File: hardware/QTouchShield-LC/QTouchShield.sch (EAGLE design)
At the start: 59 parts, among them IC1 AT32UC3C0512CJEDEC-MS-026, J1 SNS00...07, J10 CAPS08...15, J11 CAPS24...31, J12 CAPS16...23, J13 SPI-MEGA, J14 SPI-UNO, J15 COMMS Select, J16 DETECT00...15, J17 DETECT16...31, J18 JTAG, J19 TOUCH DATA, J2 SNS08...15, J3 SNS16...23, J4 SNS24...31, J5 RES00...07, J6 RES08...15, J7 RES16...23, J8 RES24...31, J9 CAPS00...07, Q1 BSS138, Q2 BSS138, Q3 BSS138, Q4 BSS138, Q5 BSS138, Q6 BSS138, U1 ARDUINO-2560-MEGA-R3-SMD, X1 Firmware Upgrade Port

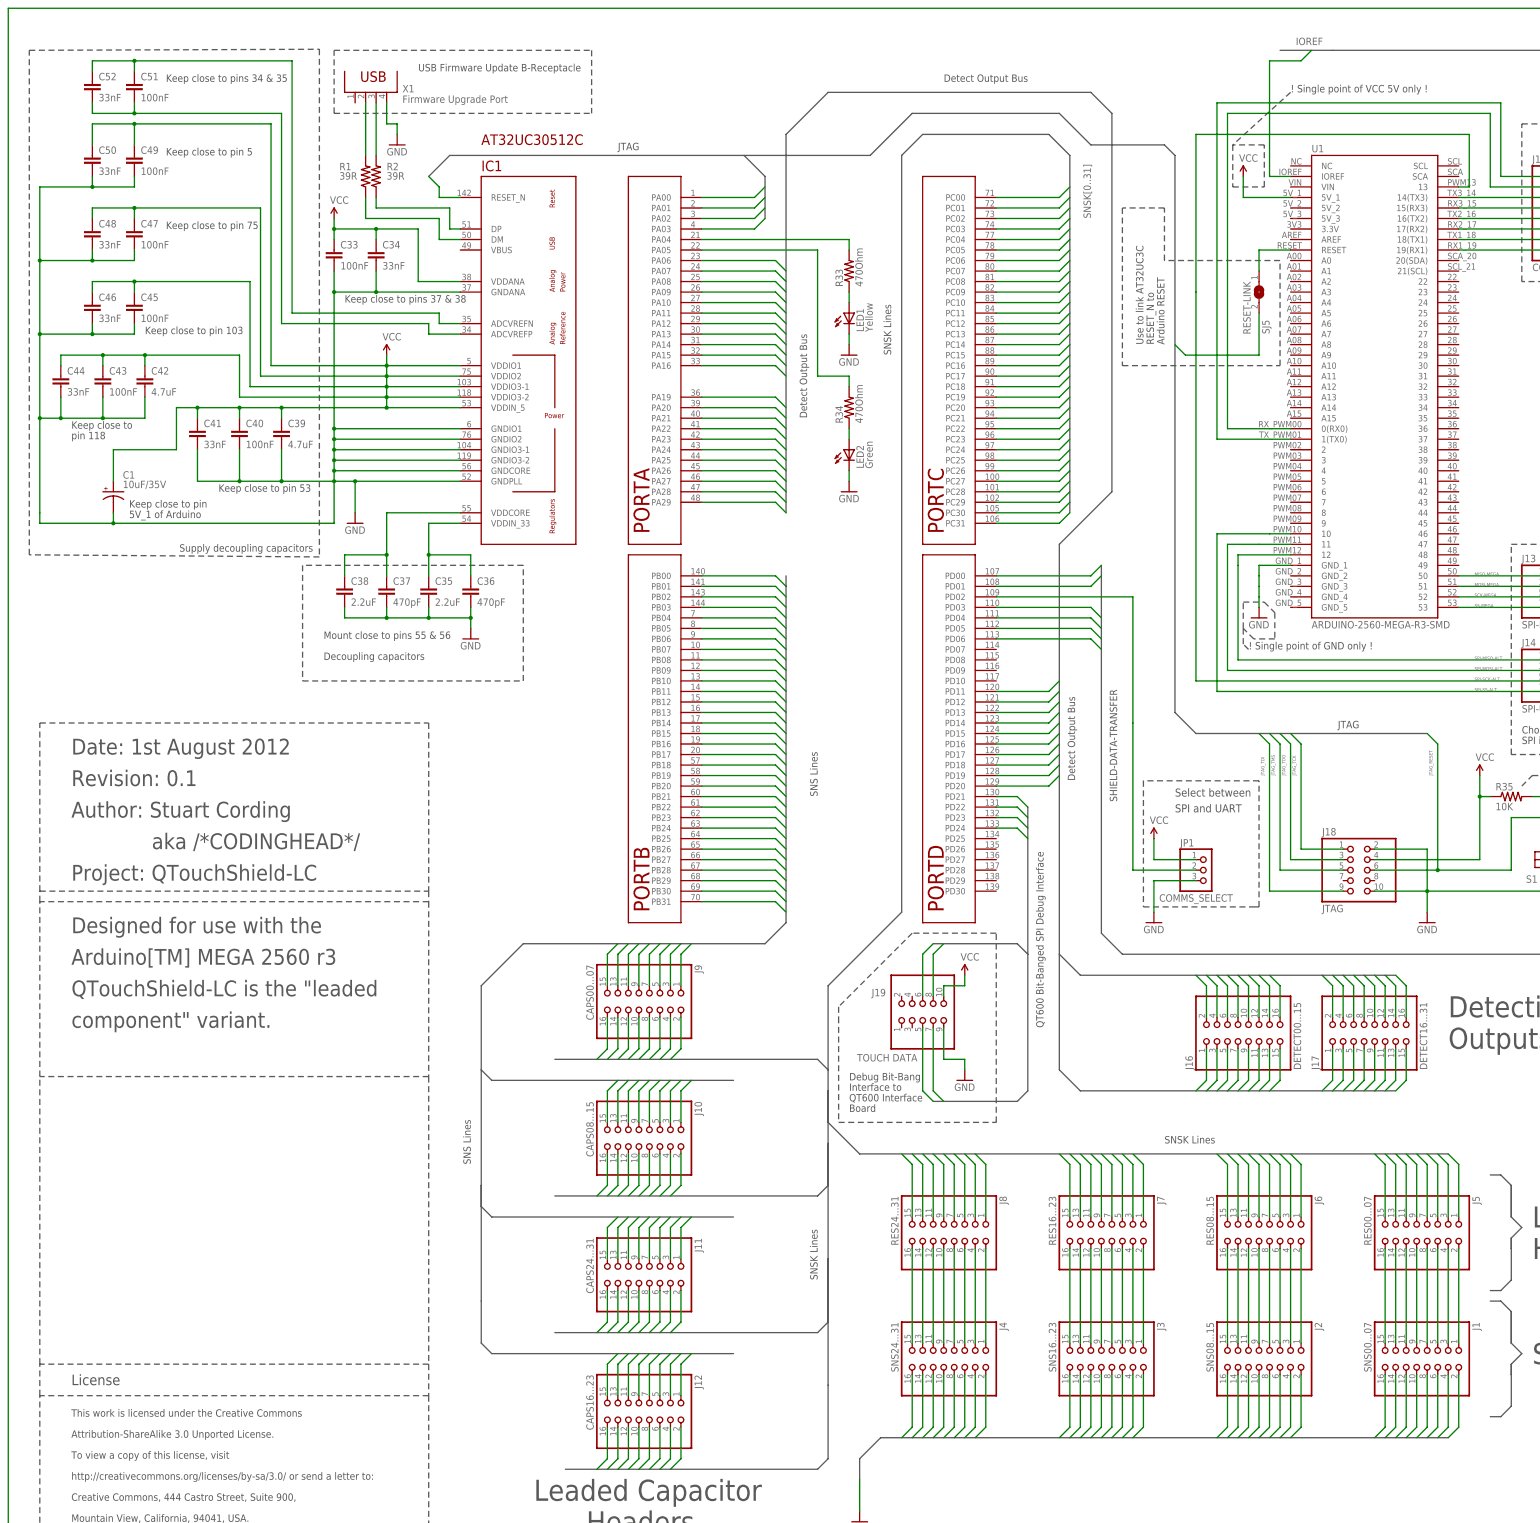
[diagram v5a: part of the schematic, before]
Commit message: Final routed board for LC version.
Board finally routed with the LC layout.
No known major issues to resolve.
Consider only ground-plane under MCU and review from STROHAL.
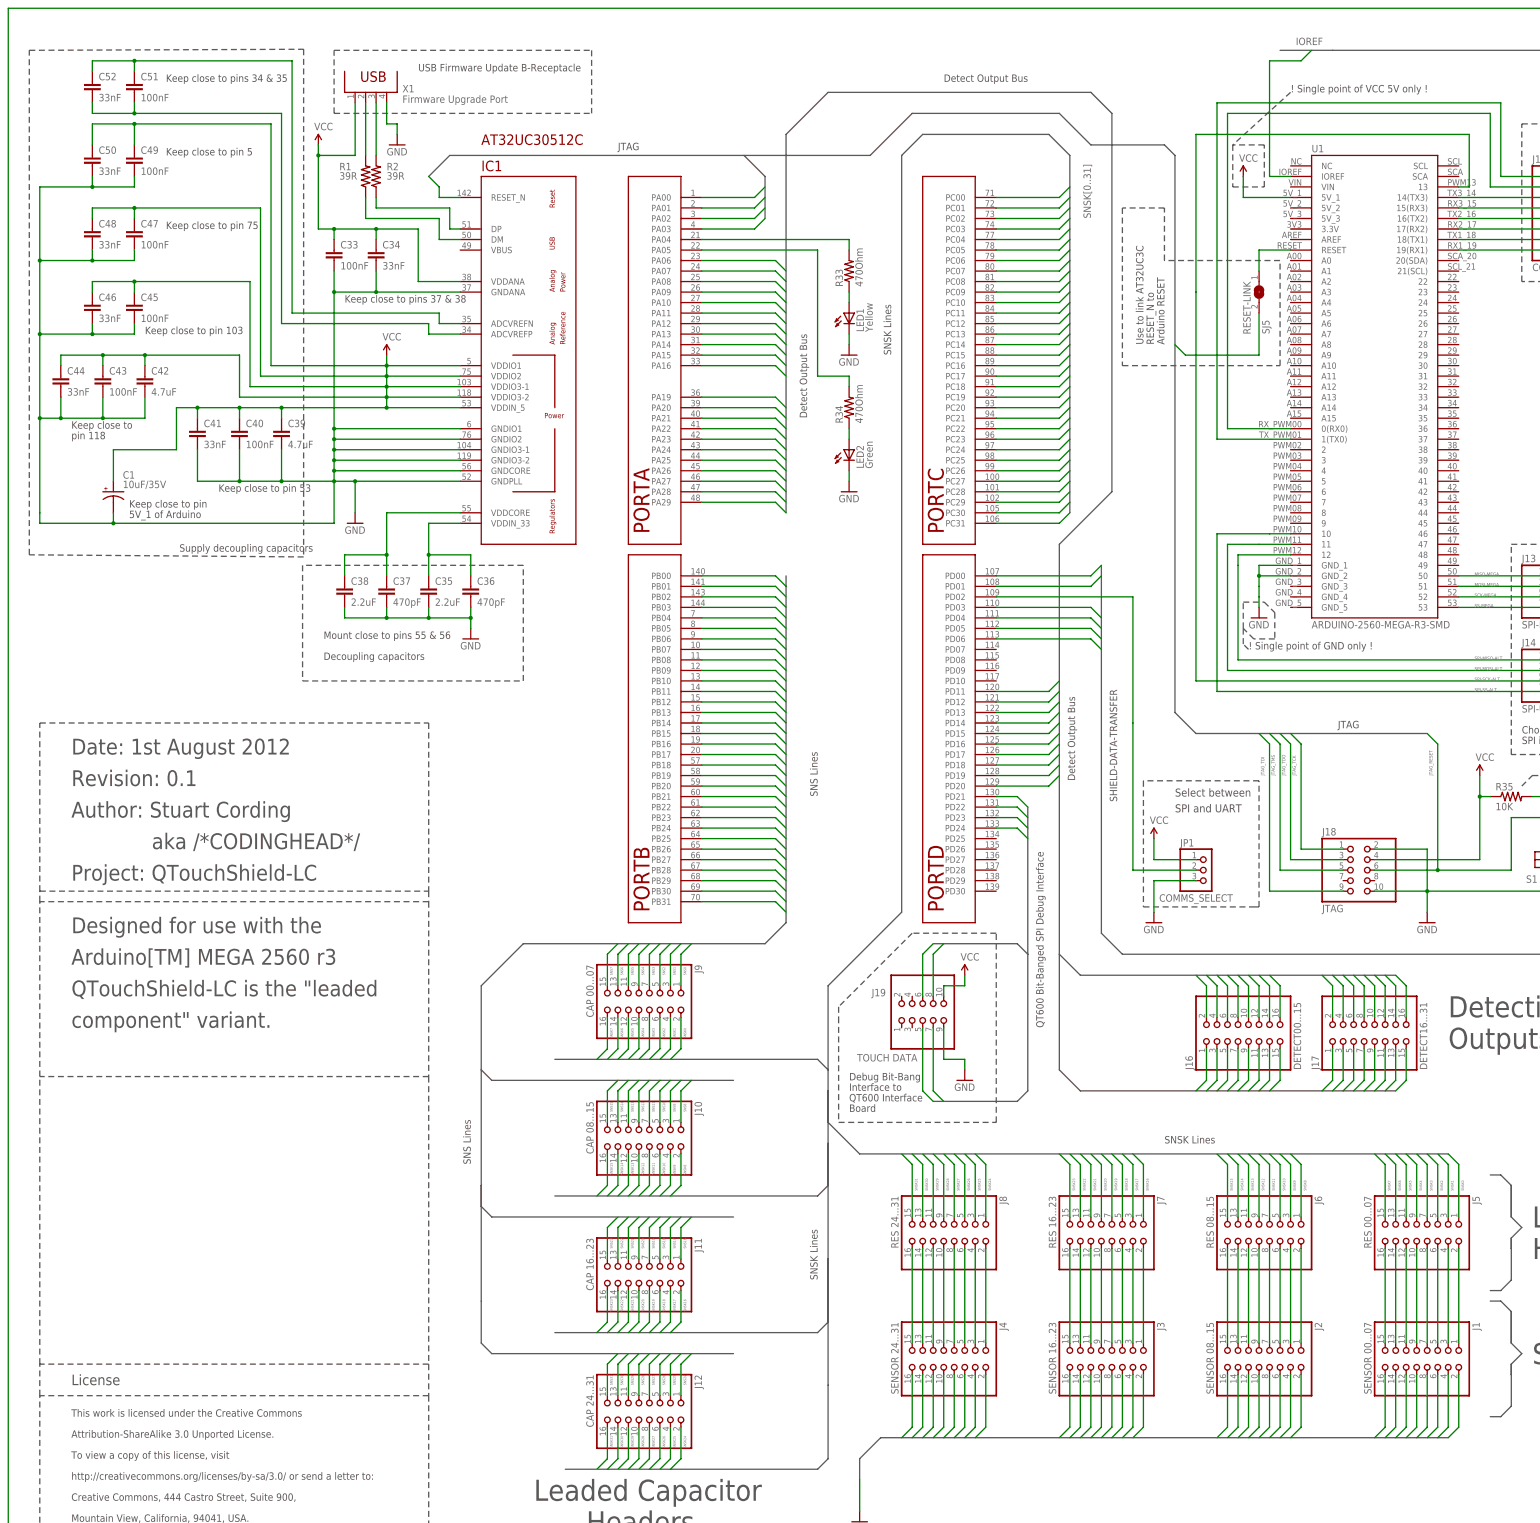
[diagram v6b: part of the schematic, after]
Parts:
- J1: value SNS00...07 -> SENSOR 00...07
- J10: value CAPS08...15 -> CAP 08...15
- J11: value CAPS24...31 -> CAP 16...23
- J12: value CAPS16...23 -> CAP 24...31
- J2: value SNS08...15 -> SENSOR 08...15
- J3: value SNS16...23 -> SENSOR 16...23
- J4: value SNS24...31 -> SENSOR 24...31
- J5: value RES00...07 -> RES 00...07
- J6: value RES08...15 -> RES 08...15
- J7: value RES16...23 -> RES 16...23
- J8: value RES24...31 -> RES 24...31
- J9: value CAPS00...07 -> CAP 00...07
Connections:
- net GND: now also U1.GND_2
- net SNS16: now also J11.1; no longer J12.15
- net SNS17: now also J11.3; no longer J12.13
- net SNS18: now also J11.5; no longer J12.11
- net SNS19: now also J11.7; no longer J12.9
- net SNS20: now also J11.9; no longer J12.7
- net SNS21: now also J11.11; no longer J12.5
- net SNS22: now also J11.13; no longer J12.3
- net SNS23: now also J11.15; no longer J12.1
- net SNS24: now also J12.1; no longer J11.15
- net SNS25: now also J12.3; no longer J11.13
- net SNS26: now also J12.5; no longer J11.11
- net SNS27: now also J12.7; no longer J11.9
- net SNS28: now also J12.9; no longer J11.7
- net SNS29: now also J12.11; no longer J11.5
- net SNS30: now also J12.13; no longer J11.3
- net SNS31: now also J12.15; no longer J11.1
- net VCC: now also X1.1

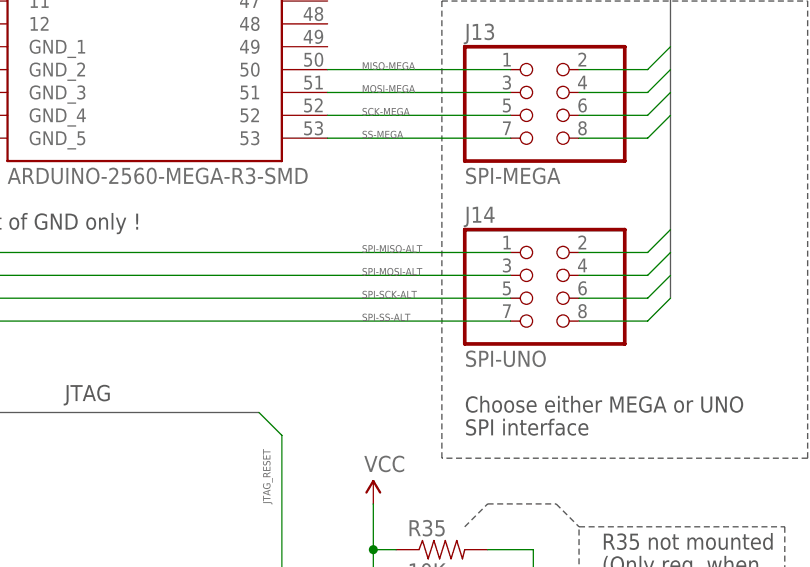
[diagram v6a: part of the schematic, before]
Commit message: Updated schematic and board, especially silk screen
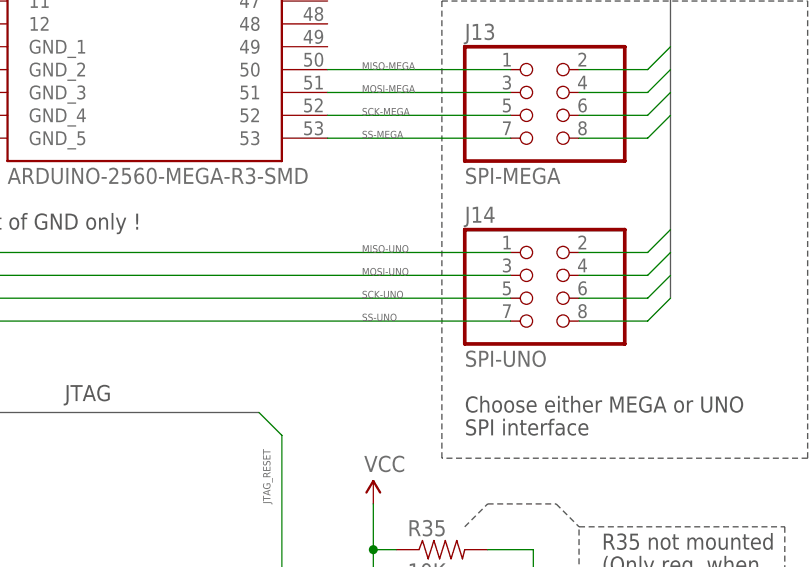
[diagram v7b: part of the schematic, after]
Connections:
- net SPI-MISO-ALT renamed MISO-UNO
- net SPI-MOSI-ALT renamed MOSI-UNO
- net SPI-SCK-ALT renamed SCK-UNO
- net SPI-SS-ALT renamed SS-UNO
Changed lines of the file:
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@@
 </segment>
 </net>
-<net name="SPI-SCK-ALT" class="0">
+<net name="SCK-UNO" class="0">
 <segment>
 <pinref part="U1" gate="A" pin="13"/>
@@
 </segment>
 </net>
-<net name="SPI-MISO-ALT" class="0">
+<net name="MISO-UNO" class="0">
 <segment>
 <pinref part="U1" gate="A" pin="12"/>
@@
 </segment>
 </net>
-<net name="SPI-MOSI-ALT" class="0">
+<net name="MOSI-UNO" class="0">
 <segment>
 <pinref part="U1" gate="A" pin="11"/>
@@
 </segment>
 </net>
-<net name="SPI-SS-ALT" class="0">
+<net name="SS-UNO" class="0">
 <segment>
 <pinref part="U1" gate="A" pin="10"/>
